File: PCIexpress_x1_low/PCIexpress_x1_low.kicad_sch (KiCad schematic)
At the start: 24 parts, among them J1 PCIexpress_bracket, J3 87832-1420, J4 PMOD_Host_Conn_02x06, J5 PMOD_Host_Conn_02x06, J6 PMOD_Host_Conn_02x06, U1 XC7A50T-CSG325, U2 LTM4643EY_PBF, U3 MX25L3233FM1

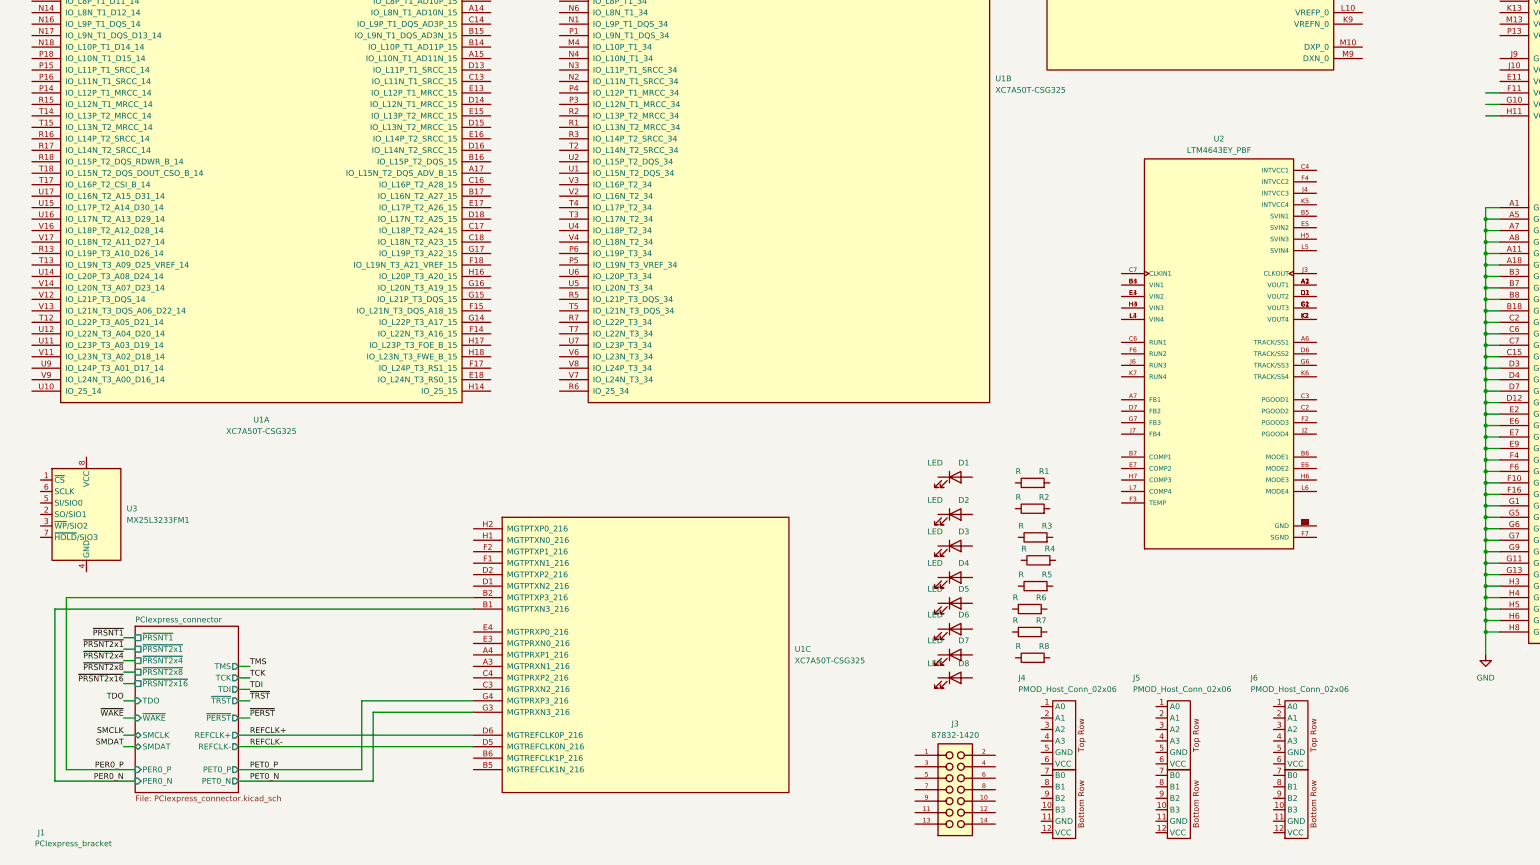
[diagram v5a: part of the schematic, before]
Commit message: adding AC coupling caps
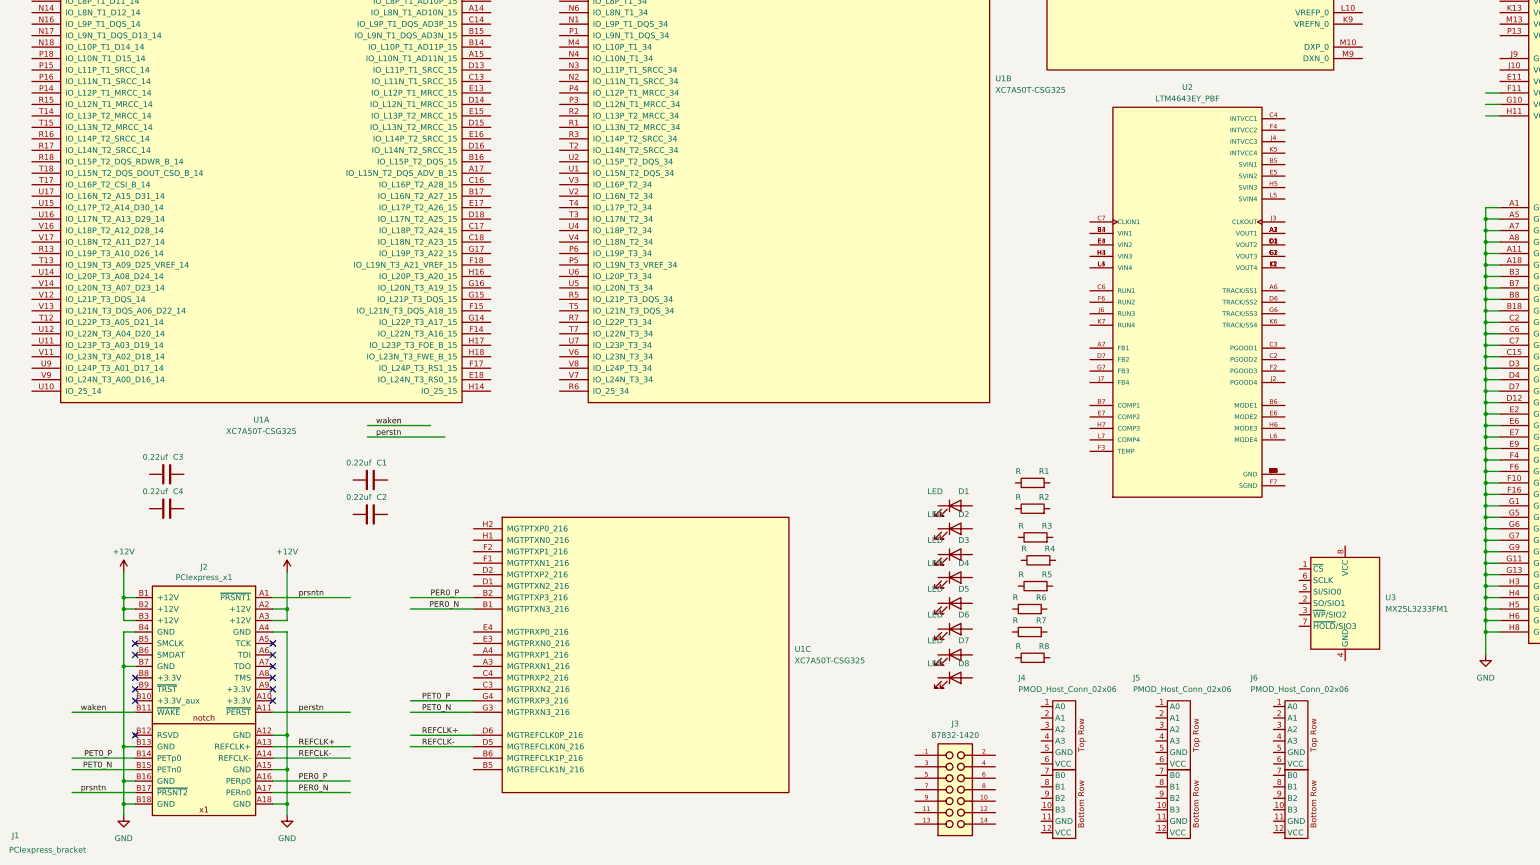
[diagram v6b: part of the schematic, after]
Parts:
- added C1, C2, C3, C4: 0.22uf, Capacitor_SMD:C_0402_1005Metric, symbol Device:C
- added J2: PCIexpress_x1, PCIexpress:PCIexpress_x1, symbol PCIexpress:PCIexpress_x1
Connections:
- net GND: now also J2.A12 (GND), J2.A15 (GND), J2.A18 (GND), J2.A4 (GND), J2.B13 (GND), J2.B16 (GND), J2.B18 (GND), J2.B4 (GND), J2.B7 (GND)
- net PER0_N: now also J2.A17 (PERn0)
- net PER0_P: now also J2.A16 (PERp0)
- net PET0_N: now also J2.B15 (PETn0)
- net PET0_P: now also J2.B14 (PETp0)
- net REFCLK+: now also J2.A13 (REFCLK+)
- net REFCLK-: now also J2.A14 (REFCLK-)
- new net +12V: J2.A2 (+12V), J2.A3 (+12V), J2.B1 (+12V), J2.B2 (+12V), J2.B3 (+12V)
- new net perstn: J2.A11 (~{PERST})
- new net prsntn: J2.A1 (~{PRSNT1}), J2.B17 (~{PRSNT2})
- new net waken: J2.B11 (~{WAKE})
- no-connect marks 0 -> 12
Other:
- removed sheet PCIexpress_connector
- moved on the sheet: D1, D2, D3, U2, U3

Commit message: using hierarchal sheets
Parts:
- removed C1, C2, C3, C4: 0.22uf, Capacitor_SMD:C_0402_1005Metric, symbol Device:C
- removed J1: PCIexpress_bracket, PCIexpress:PCIexpress_bracket_low, symbol PCIexpress:PCIexpress_bracket
- removed J2: PCIexpress_x1, PCIexpress:PCIexpress_x1, symbol PCIexpress:PCIexpress_x1
- removed U1: XC7A50T-CSG325, Package_BGA:Xilinx_CSG325, symbol FPGA_Xilinx_Artix7:XC7A50T-CSG325
- removed U2: LTM4643EY_PBF, pedrolib:BGA77C127P7X11_1500X900X262, symbol pedrolib:LTM4643EY_PBF
- removed U3: MX25L3233FM1, Package_SO:SOP-8_3.9x4.9mm_P1.27mm, symbol Memory_Flash:MX25L3233FM1
- added J7: Conn_02x04_Odd_Even, Connector_PinHeader_2.54mm:PinHeader_2x04_P2.54mm_Vertical, symbol Connector_Generic:Conn_02x04_Odd_Even
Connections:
- net GND: now also J4.11 (GND), J4.5 (GND), J5.11 (GND), J5.5 (GND), J6.11 (GND), J6.5 (GND), J7.1 (Pin_1), J7.3 (Pin_3), J7.5 (Pin_5), J7.7 (Pin_7)
- net +3V3: now reaches J5.12 (VCC)
- net +3V3: now also J4.12 (VCC), J4.6 (VCC), J5.6 (VCC), J6.12 (VCC), J6.6 (VCC)
- no-connect marks 12 -> 0
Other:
- added sheet fpga (fpga.kicad_sch)
- added sheet pcie (pcie.kicad_sch)
- added sheet power (power.kicad_sch)
- moved on the sheet: D1, D2, D3, D4, D5, D6, D7, D8, J3, J4, J5, J6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
